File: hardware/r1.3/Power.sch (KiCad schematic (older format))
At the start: 46 parts, among them J1 RPi_GPIO, P3 I2C, P4 DISPLAY, P5 STLINK, P7 CONN_02X03, P8 USB_OTG, SW1 NO, U4 LD1117S33TR

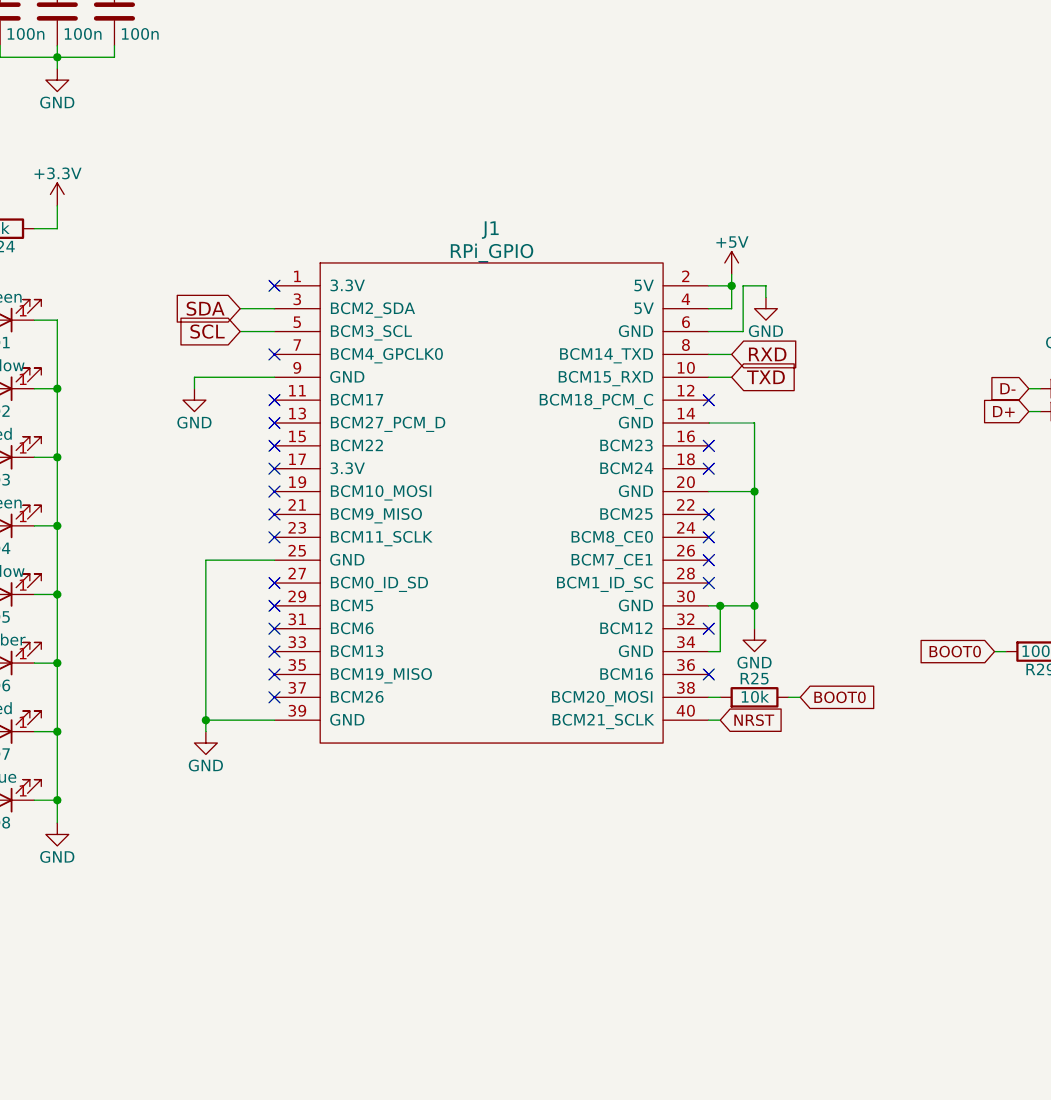
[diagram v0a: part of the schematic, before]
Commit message: Cleaned up libraries and schematics
Preparation for Revision 2.0
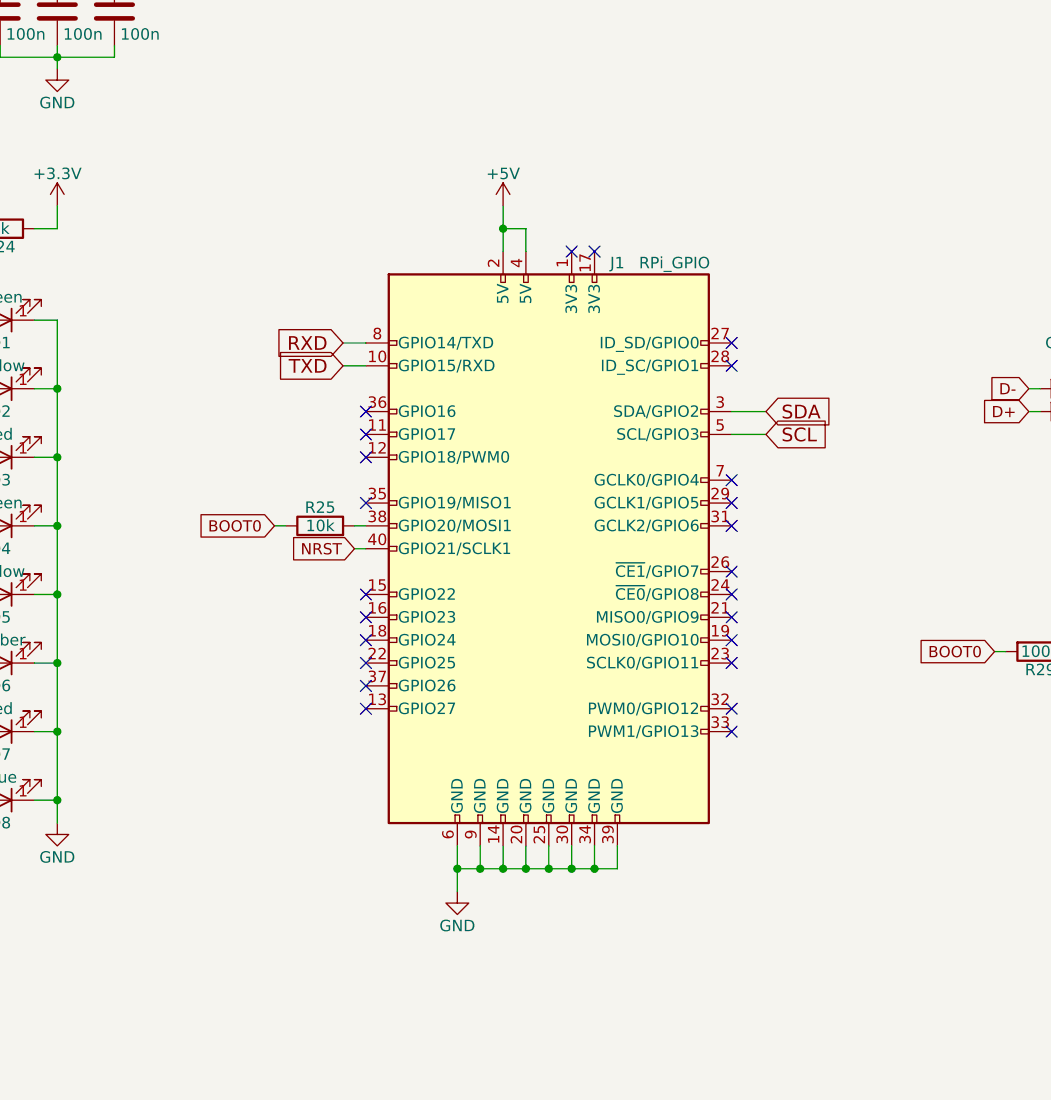
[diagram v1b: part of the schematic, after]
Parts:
- removed J1: RPi_GPIO, Pin_Headers:Pin_Header_Straight_2x20, symbol mmdvm_hs_dual_hat-rescue:RPi_GPIO-RESCUE-mmdvm_hs_dual_hat-mmdvm_hs_dual_hat-re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
- added J1: RPi_GPIO, Pin_Headers:Pin_Header_Straight_2x20, symbol Connector:Raspberry_Pi_2_3
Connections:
- net +5V: now also J1.2 (5V), J1.4 (5V)
- net GND: now also J1.14 (GND), J1.20 (GND), J1.25 (GND), J1.30 (GND), J1.34 (GND), J1.39 (GND), J1.6 (GND), J1.9 (GND)
- net NRST: now also J1.40 (GPIO21/SCLK1)
- net RXD: now also J1.8 (GPIO14/TXD)
- net SCL: now also J1.5 (SCL/GPIO3)
- net SDA: now also J1.3 (SDA/GPIO2)
- net TXD: now also J1.10 (GPIO15/RXD)
- net at R25.2: now also J1.38 (GPIO20/MOSI1)
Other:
- moved on the sheet: R25
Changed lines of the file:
@@
 EESchema Schematic File Version 4
-LIBS:mmdvm_hs_dual_hat-cache
-EELAYER 26 0
+EELAYER 30 0
 EELAYER END
 $Descr A4 11693 8268
@@
 $EndComp
 $Comp
-L mmdvm_hs_dual_hat-rescue:R-device-mmdvm_hs_dual_hat-rescue R25
-U 1 1 5A842562
-P 5350 4050
-F 0 "R25" V 5430 4050 50  0000 C CNN
-F 1 "10k" V 5350 4050 50  0000 C CNN
-F 2 "Resistors_SMD:R_0402" V 5280 4050 50  0001 C CNN
-F 3 "https://www.mouser.com/ds/2/427/crcwce3-1223726.pdf" H 5350 4050 50  0001 C CNN
-F 4 "Vishay" H 3200 200 50  0001 C CNN "MFR"
-F 5 "CRCW040210K0JNEDC" H 3200 200 50  0001 C CNN "MPN"
-F 6 "Mouser" H 3200 200 50  0001 C CNN "SPR"
-F 7 "71-CRCW040210K0JNEDC" H 3200 200 50  0001 C CNN "SPN"
-F 8 "" H 3200 200 50  0001 C CNN "SPURL"
-	1    5350 4050
-	0    1    -1   0
-$EndComp
-$Comp
 L mmdvm_hs_dual_hat-rescue:LED-RESCUE-mmdvm_hs-hat-RESCUE-mmdvm_hs_dual_hat-mmdvm_hs_dual_hat-rescue D1
 U 1 1 5A84256D
@@
 $EndComp
 $Comp
-L power:GND #PWR085
-U 1 1 5A842621
-P 2900 2700
-F 0 "#PWR085" H 2900 2450 50  0001 C CNN
-F 1 "GND" H 2900 2550 50  0000 C CNN
-F 2 "" H 2900 2700 50  0000 C CNN
-F 3 "" H 2900 2700 50  0000 C CNN
-	1    2900 2700
-	1    0    0    -1
-$EndComp
-$Comp
-L power:GND #PWR086
-U 1 1 5A842627
-P 2950 4200
-F 0 "#PWR086" H 2950 3950 50  0001 C CNN
-F 1 "GND" H 2950 4050 50  0000 C CNN
-F 2 "" H 2950 4200 50  0000 C CNN
-F 3 "" H 2950 4200 50  0000 C CNN
-	1    2950 4200
-	1    0    0    -1
-$EndComp
-$Comp
-L power:GND #PWR089
-U 1 1 5A84262D
-P 5400 2300
-F 0 "#PWR089" H 5400 2050 50  0001 C CNN
-F 1 "GND" H 5400 2150 50  0000 C CNN
-F 2 "" H 5400 2300 50  0000 C CNN
-F 3 "" H 5400 2300 50  0000 C CNN
-	1    5400 2300
-	1    0    0    -1
-$EndComp
-$Comp
-L power:GND #PWR088
-U 1 1 5A842633
-P 5350 3750
-F 0 "#PWR088" H 5350 3500 50  0001 C CNN
-F 1 "GND" H 5350 3600 50  0000 C CNN
-F 2 "" H 5350 3750 50  0000 C CNN
-F 3 "" H 5350 3750 50  0000 C CNN
-	1    5350 3750
-	1    0    0    -1
-$EndComp
-$Comp
-L power:+5V #PWR087
-U 1 1 5A842639
-P 5250 2200
-F 0 "#PWR087" H 5250 2050 50  0001 C CNN
-F 1 "+5V" H 5250 2340 50  0000 C CNN
-F 2 "" H 5250 2200 50  0000 C CNN
-F 3 "" H 5250 2200 50  0000 C CNN
-	1    5250 2200
-	1    0    0    -1
-$EndComp
-$Comp
 L mmdvm_hs_dual_hat-rescue:LED-RESCUE-mmdvm_hs-hat-RESCUE-mmdvm_hs_dual_hat-mmdvm_hs_dual_hat-rescue D0
 U 1 1 5A842643
@@
 $EndComp
 $Comp
-L mmdvm_hs_dual_hat-rescue:RPi_GPIO-RESCUE-mmdvm_hs_dual_hat-mmdvm_hs_dual_hat-rescue J1
-U 1 1 5A8426B4
-P 3450 2250
-F 0 "J1" H 4200 2500 60  0000 C CNN
-F 1 "RPi_GPIO" H 4200 2400 60  0000 C CNN
-F 2 "Pin_Headers:Pin_Header_Straight_2x20" H 3450 2250 60  0001 C CNN
-F 3 "https://www.mouser.com/ds/2/181/M20-783-1133465.pdf" H 3450 2250 60  0001 C CNN
-F 4 "Harwin" H 0   0   50  0001 C CNN "MFR"
-F 5 "M20-7832046" H 0   0   50  0001 C CNN "MPN"
-F 6 "Mouser" H 0   0   50  0001 C CNN "SPR"
-F 7 "855-M20-7832046" H 0   0   50  0001 C CNN "SPN"
-F 8 "" H 0   0   50  0001 C CNN "SPURL"
-	1    3450 2250
-	1    0    0    -1
-$EndComp
-$Comp
 L power:+3.3V #PWR080
 U 1 1 5A8426BC
@@
 Text GLabel 1500 850  2    49   Input ~ 0
 NRST
-Text GLabel 5550 4050 2    49   Input ~ 0
-BOOT0
 Text GLabel 1400 2700 0    49   Input ~ 0
 COS_LED
@@
 Text GLabel 1400 3900 0    49   Input ~ 0
 YSF_LED
-Text GLabel 5250 2550 2    60   Input ~ 0
-RXD
-Text GLabel 5250 2650 2    60   Input ~ 0
-TXD
-Text GLabel 5200 4150 2    49   Input ~ 0
-NRST
 Text GLabel 1400 2000 0    49   Input ~ 0
 SERVICE
-Text GLabel 3100 2350 0    60   Input ~ 0
-SDA
-Text GLabel 3100 2450 0    60   Input ~ 0
-SCL
 Text GLabel 1400 4500 0    49   Input ~ 0
 NXDN_LED
@@
 	1400 2400 1500 2400
 Wire Wire Line
-	2900 2650 3250 2650
-Wire Wire Line
-	3250 4150 2950 4150
-Wire Wire Line
-	2900 2650 2900 2700
-Wire Wire Line
-	3250 3450 2950 3450
-Wire Wire Line
 	1400 2000 1500 2000
 Wire Wire Line
@@
 	1800 2400 1900 2400
 Wire Wire Line
-	2950 3450 2950 4150
-Wire Wire Line
-	3250 2350 3100 2350
-Wire Wire Line
-	3250 2450 3100 2450
-Wire Wire Line
-	5150 2850 5350 2850
-Wire Wire Line
-	5150 3650 5200 3650
-Wire Wire Line
-	5150 3150 5350 3150
-Wire Wire Line
-	5150 3850 5200 3850
-Wire Wire Line
-	5200 3850 5200 3650
-Wire Wire Line
-	5350 2850 5350 3150
-Wire Wire Line
-	5150 4050 5200 4050
-Wire Wire Line
-	5500 4050 5550 4050
-Wire Wire Line
-	5150 2650 5250 2650
-Wire Wire Line
-	5400 2250 5300 2250
-Wire Wire Line
-	5300 2250 5300 2450
-Wire Wire Line
 	1900 4500 1800 4500
 Wire Wire Line
@@
 	2300 3900 2300 4200
 Wire Wire Line
-	2950 4150 2950 4200
-Wire Wire Line
-	5350 3650 5350 3750
-Wire Wire Line
-	5350 3150 5350 3650
-Wire Wire Line
-	5200 3650 5350 3650
-Wire Wire Line
 	2200 4500 2300 4500
 Wire Wire Line
 	2300 4500 2300 4600
 Wire Wire Line
-	5150 2350 5250 2350
-Wire Wire Line
-	5250 2350 5250 2250
-Wire Wire Line
-	5150 2250 5250 2250
-Wire Wire Line
-	5250 2250 5250 2200
-Wire Wire Line
 	2300 4200 2300 4500
-Wire Wire Line
-	5300 2450 5150 2450
-Wire Wire Line
-	5400 2300 5400 2250
-Wire Wire Line
-	5150 2550 5250 2550
-Wire Wire Line
-	5150 4150 5200 4150
 Wire Wire Line
 	6900 2800 6950 2800
@@
 Connection ~ 2300 3900
 Connection ~ 2300 4200
-Connection ~ 2950 4150
-Connection ~ 5350 3650
-Connection ~ 5350 3150
-Connection ~ 5200 3650
 Connection ~ 2300 4500
-Connection ~ 5250 2250
 Connection ~ 7350 2800
 Connection ~ 6950 2700
@@
 Connection ~ 10100 2950
 Connection ~ 7600 3850
-NoConn ~ 3250 2550
-NoConn ~ 3250 2750
-NoConn ~ 3250 2850
-NoConn ~ 3250 2950
-NoConn ~ 3250 3150
-NoConn ~ 3250 3250
-NoConn ~ 3250 3350
-NoConn ~ 3250 3550
-NoConn ~ 3250 3650
-NoConn ~ 3250 3750
-NoConn ~ 3250 3850
-NoConn ~ 3250 3950
-NoConn ~ 3250 4050
-NoConn ~ 5150 3950
-NoConn ~ 5150 3750
-NoConn ~ 5150 3550
-NoConn ~ 5150 3450
-NoConn ~ 5150 3350
-NoConn ~ 5150 3250
-NoConn ~ 5150 3050
-NoConn ~ 5150 2950
-NoConn ~ 5150 2750
-NoConn ~ 3250 2250
-NoConn ~ 3250 3050
 NoConn ~ 7400 2900
 Wire Wire Line
@@
 Wire Wire Line
 	1400 7300 1550 7300
+$Comp
+L mmdvm_hs_dual_hat-rescue:R-device-mmdvm_hs_dual_hat-rescue R25
+U 1 1 5A842562
+P 3450 3300
+F 0 "R25" V 3530 3300 50  0000 C CNN
+F 1 "10k" V 3450 3300 50  0000 C CNN
+F 2 "Resistors_SMD:R_0402" V 3380 3300 50  0001 C CNN
+F 3 "https://www.mouser.com/ds/2/427/crcwce3-1223726.pdf" H 3450 3300 50  0001 C CNN
+F 4 "Vishay" H 1300 -550 50  0001 C CNN "MFR"
+F 5 "CRCW040210K0JNEDC" H 1300 -550 50  0001 C CNN "MPN"
+F 6 "Mouser" H 1300 -550 50  0001 C CNN "SPR"
+F 7 "71-CRCW040210K0JNEDC" H 1300 -550 50  0001 C CNN "SPN"
+F 8 "" H 1300 -550 50  0001 C CNN "SPURL"
+	1    3450 3300
+	0    -1   -1   0
+$EndComp
+$Comp
+L power:GND #PWR086
+U 1 1 5A842627
+P 4050 4900
+F 0 "#PWR086" H 4050 4650 50  0001 C CNN
+F 1 "GND" H 4050 4750 50  0000 C CNN
+F 2 "" H 4050 4900 50  0000 C CNN
+F 3 "" H 4050 4900 50  0000 C CNN
+	1    4050 4900
+	1    0    0    -1
+$EndComp
+$Comp
+L power:+5V #PWR087
+U 1 1 5A842639
+P 4250 1900
+F 0 "#PWR087" H 4250 1750 50  0001 C CNN
+F 1 "+5V" H 4250 2040 50  0000 C CNN
+F 2 "" H 4250 1900 50  0000 C CNN
+F 3 "" H 4250 1900 50  0000 C CNN
+	1    4250 1900
+	1    0    0    -1
+$EndComp
+Text GLabel 3250 3300 0    49   Input ~ 0
+BOOT0
+Text GLabel 3550 2500 0    60   Input ~ 0
+RXD
+Text GLabel 3550 2600 0    60   Input ~ 0
+TXD
+Text GLabel 3600 3400 0    49   Input ~ 0
+NRST
+Text GLabel 5400 2800 2    60   Input ~ 0
+SDA
+Text GLabel 5400 2900 2    60   Input ~ 0
+SCL
+Wire Wire Line
+	5250 2800 5400 2800
+Wire Wire Line
+	5250 2900 5400 2900
+Wire Wire Line
+	3650 3300 3600 3300
+Wire Wire Line
+	3300 3300 3250 3300
+Wire Wire Line
+	3650 2600 3550 2600
+Wire Wire Line
+	3650 2500 3550 2500
+Wire Wire Line
+	3650 3400 3600 3400
+$Comp
+L Connector:Raspberry_Pi_2_3 J1
+U 1 1 5F40DFA0
+P 4450 3400
+F 0 "J1" H 4750 4650 50  0000 C CNN
+F 1 "RPi_GPIO" H 5000 4650 50  0000 C CNN
+F 2 "Pin_Headers:Pin_Header_Straight_2x20" H 4450 3400 50  0001 C CNN
+F 3 "https://www.raspberrypi.org/documentation/hardware/raspberrypi/schematics/rpi_SCH_3bplus_1p0_reduced.pdf" H 4450 3400 50  0001 C CNN
+	1    4450 3400
+	1    0    0    -1
+$EndComp
+Wire Wire Line
+	4050 4700 4050 4800
+Wire Wire Line
+	4050 4800 4150 4800
+Wire Wire Line
+	4750 4800 4750 4700
+Wire Wire Line
+	4650 4700 4650 4800
+Connection ~ 4650 4800
+Wire Wire Line
+	4650 4800 4750 4800
+Wire Wire Line
+	4550 4700 4550 4800
+Connection ~ 4550 4800
+Wire Wire Line
+	4550 4800 4650 4800
+Wire Wire Line
+	4450 4700 4450 4800
+Connection ~ 4450 4800
+Wire Wire Line
+	4450 4800 4550 4800
+Wire Wire Line
+	4350 4700 4350 4800
+Connection ~ 4350 4800
+Wire Wire Line
+	4350 4800 4450 4800
+Wire Wire Line
+	4250 4700 4250 4800
+Connection ~ 4250 4800
+Wire Wire Line
+	4250 4800 4350 4800
+Wire Wire Line
+	4150 4700 4150 4800
+Connection ~ 4150 4800
+Wire Wire Line
+	4150 4800 4250 4800
+Wire Wire Line
+	4050 4800 4050 4900
+Connection ~ 4050 4800
+NoConn ~ 4550 2100
+NoConn ~ 4650 2100
+Wire Wire Line
+	4250 1900 4250 2000
+Wire Wire Line
+	4250 2000 4350 2000
+Wire Wire Line
+	4350 2000 4350 2100
+Connection ~ 4250 2000
+Wire Wire Line
+	4250 2000 4250 2100
+NoConn ~ 3650 2800
+NoConn ~ 3650 2900
+NoConn ~ 3650 3000
+NoConn ~ 3650 3200
+NoConn ~ 3650 3600
+NoConn ~ 3650 3700
+NoConn ~ 3650 3800
+NoConn ~ 3650 3900
+NoConn ~ 3650 4000
+NoConn ~ 3650 4100
+NoConn ~ 5250 4200
+NoConn ~ 5250 4100
+NoConn ~ 5250 3900
+NoConn ~ 5250 3800
+NoConn ~ 5250 3700
+NoConn ~ 5250 3600
+NoConn ~ 5250 3500
+NoConn ~ 5250 3300
+NoConn ~ 5250 3200
+NoConn ~ 5250 3100
+NoConn ~ 5250 2600
+NoConn ~ 5250 2500
 $EndSCHEMATC
